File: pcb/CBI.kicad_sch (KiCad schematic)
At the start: 87 parts, among them J1 Conn_01x03_Socket, J11 Screw_Terminal_01x03, J12 Conn_01x04_Pin, J4 Conn_01x02_Socket, J5 Conn_01x02_Socket, J6 Conn_01x03_Socket, J7 Conn_01x03_Socket, J9 Conn_01x02_Socket, J99 Conn_01x03_Socket, Q1 BC817, Q11 MMBFJ113, Q12 MMBFJ113, Q13 MMBFJ113, Q14 AO3416A, Q15 AO3416A, Q2 BC817, Q3 MMBFJ113, Q4 MMBFJ113, Q5 AO3416A, Q6 AO3416A, SW1 SW_SPST, U1 CNY17-4, U2 CNY17-4, U3 MCP23008-xSO

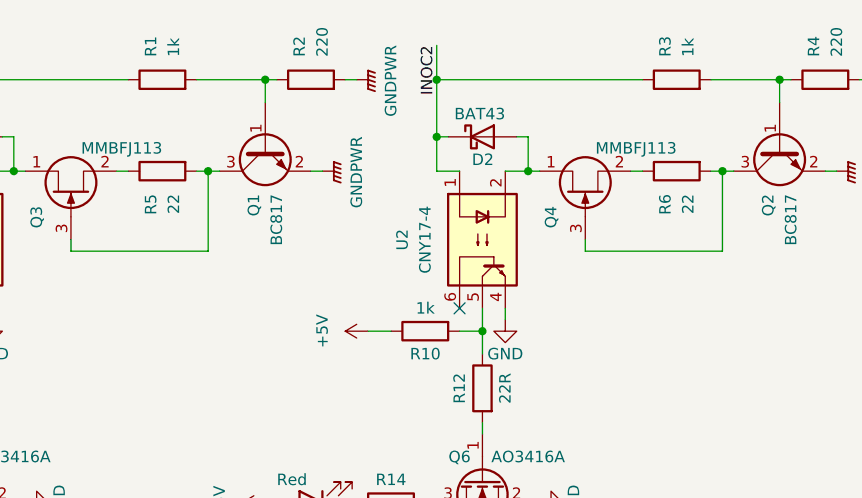
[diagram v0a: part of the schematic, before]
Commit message: Add missing vendor(id)
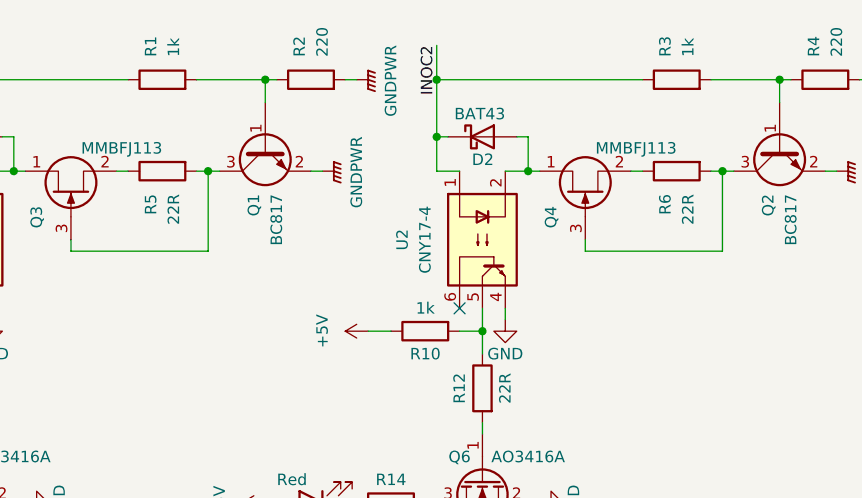
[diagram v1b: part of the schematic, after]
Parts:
- D20, D21, D22, D23: Vendor (none) -> HTL; VendorId (none) -> 100187
- J11: Vendor (none) -> DigiKey; VendorId (none) -> 277-1151-ND, 277-1012-ND
- Q1, Q2: Vendor (none) -> HTL; VendorId (none) -> 103452
- R1, R22, R24, R26, R28, R3: VendorId 102938 -> 102951
- R10, R9: VendorId 102940 -> 102951
- R11, R12: VendorId 102940 -> 102919
- R2, R4: VendorId 102938 -> 102937
- R5, R6: value 22 -> 22R; VendorId 102938 -> 102919
- U1, U2: Vendor (none) -> DigiKey; VendorId (none) -> 160-1323-5-ND
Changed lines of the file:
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@@
       (effects (font (size 1.27 1.27)) hide)
     )
-    (property "VendorId" "102938" (at 207.01 25.4 0)
+    (property "VendorId" "102937" (at 207.01 25.4 0)
       (effects (font (size 1.27 1.27)) hide)
     )
@@
       (effects (font (size 1.27 1.27)) hide)
     )
-    (property "VendorId" "102940" (at 162.56 53.34 0)
+    (property "VendorId" "102951" (at 162.56 53.34 0)
       (effects (font (size 1.27 1.27)) hide)
     )
@@
       (effects (font (size 1.27 1.27)) hide)
     )
-    (property "VendorId" "102940" (at 168.91 59.69 0)
+    (property "VendorId" "102919" (at 168.91 59.69 0)
       (effects (font (size 1.27 1.27)) hide)
     )
@@
       (effects (font (size 1.27 1.27)) hide)
     )
+    (property "Vendor" "HTL" (at 210.82 97.79 0)
+      (effects (font (size 1.27 1.27)) hide)
+    )
+    (property "VendorId" "100187" (at 210.82 97.79 0)
+      (effects (font (size 1.27 1.27)) hide)
+    )
     (pin "1")
     (pin "2")
@@
       (effects (font (size 1.27 1.27)) hide)
     )
+    (property "Vendor" "DigiKey" (at 125.73 25.4 0)
+      (effects (font (size 1.27 1.27)) hide)
+    )
+    (property "VendorId" "277-1151-ND, 277-1012-ND" (at 125.73 25.4 0)
+      (effects (font (size 1.27 1.27)) hide)
+    )
     (pin "1")
     (pin "3")
@@
       (effects (font (size 1.27 1.27)) (justify left) hide)
     )
+    (property "Vendor" "HTL" (at 201.93 33.02 0)
+      (effects (font (size 1.27 1.27)) hide)
+    )
+    (property "VendorId" "103452" (at 201.93 33.02 0)
+      (effects (font (size 1.27 1.27)) hide)
+    )
     (pin "1")
     (pin "2")
@@
       (effects (font (size 1.27 1.27)) hide)
     )
-    (property "VendorId" "102938" (at 168.91 97.79 0)
+    (property "VendorId" "102951" (at 168.91 97.79 0)
       (effects (font (size 1.27 1.27)) hide)
     )
@@
       (effects (font (size 1.27 1.27)) hide)
     )
-    (property "VendorId" "102938" (at 232.41 97.79 0)
+    (property "VendorId" "102951" (at 232.41 97.79 0)
       (effects (font (size 1.27 1.27)) hide)
     )
@@
       (effects (font (size 1.27 1.27)) hide)
     )
+    (property "Vendor" "HTL" (at 147.32 97.79 0)
+      (effects (font (size 1.27 1.27)) hide)
+    )
+    (property "VendorId" "100187" (at 147.32 97.79 0)
+      (effects (font (size 1.27 1.27)) hide)
+    )
     (pin "1")
     (pin "2")
@@
       (effects (font (size 1.27 1.27)) (justify left))
     )
-    (property "Value" "22" (at 248.92 38.1 0)
+    (property "Value" "22R" (at 248.92 38.1 0)
       (effects (font (size 1.27 1.27)) (justify left))
     )
@@
       (effects (font (size 1.27 1.27)) hide)
     )
-    (property "VendorId" "102938" (at 247.65 35.56 0)
+    (property "VendorId" "102919" (at 247.65 35.56 0)
       (effects (font (size 1.27 1.27)) hide)
     )
@@
       (effects (font (size 1.27 1.27)) hide)
     )
-    (property "VendorId" "102938" (at 137.16 97.79 0)
+    (property "VendorId" "102951" (at 137.16 97.79 0)
       (effects (font (size 1.27 1.27)) hide)
     )
@@
       (effects (font (size 1.27 1.27)) hide)
     )
-    (property "VendorId" "102938" (at 190.5 25.4 0)
+    (property "VendorId" "102951" (at 190.5 25.4 0)
       (effects (font (size 1.27 1.27)) hide)
     )
@@
       (effects (font (size 1.27 1.27)) hide)
     )
-    (property "VendorId" "102938" (at 264.16 25.4 0)
+    (property "VendorId" "102937" (at 264.16 25.4 0)
       (effects (font (size 1.27 1.27)) hide)
     )
@@
       (effects (font (size 1.27 1.27)) (justify left) hide)
     )
+    (property "Vendor" "DigiKey" (at 226.06 43.18 0)
+      (effects (font (size 1.27 1.27)) hide)
+    )
+    (property "VendorId" "160-1323-5-ND" (at 226.06 43.18 0)
+      (effects (font (size 1.27 1.27)) hide)
+    )
     (pin "1")
     (pin "5")
@@
       (effects (font (size 1.27 1.27)) (justify left) hide)
     )
+    (property "Vendor" "HTL" (at 259.08 33.02 0)
+      (effects (font (size 1.27 1.27)) hide)
+    )
+    (property "VendorId" "103452" (at 259.08 33.02 0)
+      (effects (font (size 1.27 1.27)) hide)
+    )
     (pin "1")
     (pin "2")
@@
       (effects (font (size 1.27 1.27)) hide)
     )
-    (property "VendorId" "102940" (at 226.06 59.69 0)
+    (property "VendorId" "102919" (at 226.06 59.69 0)
       (effects (font (size 1.27 1.27)) hide)
     )
@@
       (effects (font (size 1.27 1.27)) hide)
     )
+    (property "Vendor" "HTL" (at 179.07 97.79 0)
+      (effects (font (size 1.27 1.27)) hide)
+    )
+    (property "VendorId" "100187" (at 179.07 97.79 0)
+      (effects (font (size 1.27 1.27)) hide)
+    )
     (pin "1")
     (pin "2")
@@
       (effects (font (size 1.27 1.27)) hide)
     )
-    (property "VendorId" "102938" (at 247.65 25.4 0)
+    (property "VendorId" "102951" (at 247.65 25.4 0)
       (effects (font (size 1.27 1.27)) hide)
     )
@@
       (effects (font (size 1.27 1.27)) (justify left) hide)
     )
+    (property "Vendor" "DigiKey" (at 168.91 43.18 0)
+      (effects (font (size 1.27 1.27)) hide)
+    )
+    (property "VendorId" "160-1323-5-ND" (at 168.91 43.18 0)
+      (effects (font (size 1.27 1.27)) hide)
+    )
     (pin "1")
     (pin "5")
@@
       (effects (font (size 1.27 1.27)) hide)
     )
-    (property "VendorId" "102940" (at 219.71 53.34 0)
+    (property "VendorId" "102951" (at 219.71 53.34 0)
       (effects (font (size 1.27 1.27)) hide)
     )
@@
       (effects (font (size 1.27 1.27)) (justify left))
     )
-    (property "Value" "22" (at 191.77 38.1 0)
+    (property "Value" "22R" (at 191.77 38.1 0)
       (effects (font (size 1.27 1.27)) (justify left))
     )
@@
       (effects (font (size 1.27 1.27)) hide)
     )
-    (property "VendorId" "102938" (at 190.5 35.56 0)
+    (property "VendorId" "102919" (at 190.5 35.56 0)
       (effects (font (size 1.27 1.27)) hide)
     )
@@
       (effects (font (size 1.27 1.27)) hide)
     )
-    (property "VendorId" "102938" (at 200.66 97.79 0)
+    (property "VendorId" "102951" (at 200.66 97.79 0)
       (effects (font (size 1.27 1.27)) hide)
     )
@@
       (effects (font (size 1.27 1.27)) hide)
     )
+    (property "Vendor" "HTL" (at 242.57 97.79 0)
+      (effects (font (size 1.27 1.27)) hide)
+    )
+    (property "VendorId" "100187" (at 242.57 97.79 0)
+      (effects (font (size 1.27 1.27)) hide)
+    )
